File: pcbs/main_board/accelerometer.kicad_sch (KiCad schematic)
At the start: 3 parts, among them U2 ADXL345

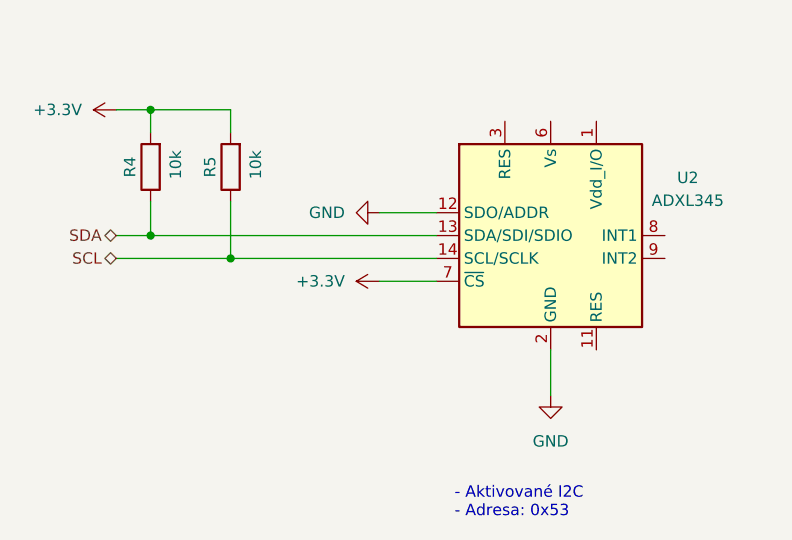
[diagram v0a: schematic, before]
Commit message: Add led strip wiring
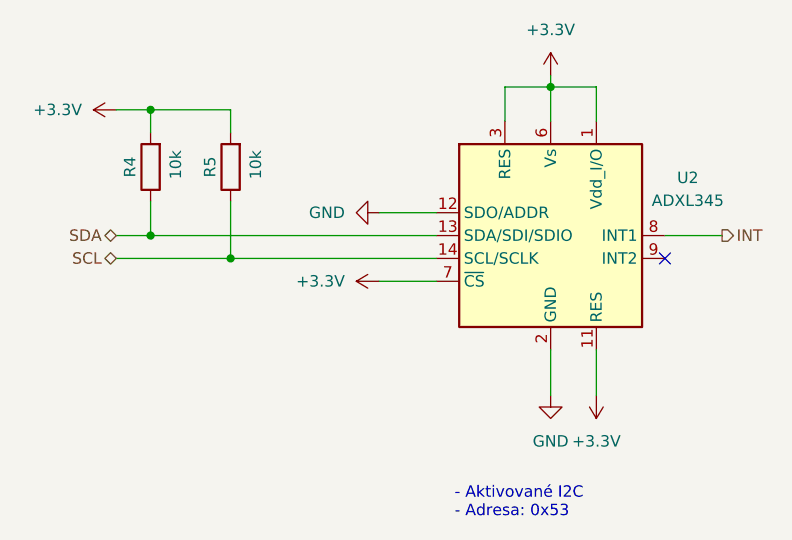
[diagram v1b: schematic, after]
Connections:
- net +3.3V: now also U2.1 (Vdd_I/O), U2.11 (RES), U2.3 (RES), U2.6 (Vs)
- net INT: now reaches U2.8 (INT1)
- no-connect marks 0 -> 1
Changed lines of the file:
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@@
+	)
+	(junction
+		(at 87.63 29.21)
+		(diameter 0)
+		(color 0 0 0 0)
 	)
 	(junction
@@
 		(color 0 0 0 0)
 	)
+	(no_connect
+		(at 100.33 48.26)
+	)
 	(wire
 		(pts
@@
 	(wire
 		(pts
+			(xy 82.55 29.21) (xy 87.63 29.21)
+		)
+		(stroke
+			(width 0)
+			(type default)
+		)
+	)
+	(wire
+		(pts
 			(xy 68.58 50.8) (xy 74.93 50.8)
 		)
@@
 	(wire
 		(pts
+			(xy 82.55 33.02) (xy 82.55 29.21)
+		)
+		(stroke
+			(width 0)
+			(type default)
+		)
+	)
+	(wire
+		(pts
 			(xy 68.58 43.18) (xy 74.93 43.18)
 		)
@@
 	(wire
 		(pts
+			(xy 92.71 58.42) (xy 92.71 63.5)
+		)
+		(stroke
+			(width 0)
+			(type default)
+		)
+	)
+	(wire
+		(pts
 			(xy 87.63 58.42) (xy 87.63 63.5)
 		)
@@
 	(wire
 		(pts
+			(xy 87.63 27.94) (xy 87.63 29.21)
+		)
+		(stroke
+			(width 0)
+			(type default)
+		)
+	)
+	(wire
+		(pts
+			(xy 92.71 33.02) (xy 92.71 29.21)
+		)
+		(stroke
+			(width 0)
+			(type default)
+		)
+	)
+	(wire
+		(pts
 			(xy 39.37 31.75) (xy 43.18 31.75)
 		)
@@
 	(wire
 		(pts
+			(xy 87.63 29.21) (xy 87.63 33.02)
+		)
+		(stroke
+			(width 0)
+			(type default)
+		)
+	)
+	(wire
+		(pts
 			(xy 43.18 41.91) (xy 43.18 45.72)
 		)
@@
 	(wire
 		(pts
+			(xy 100.33 45.72) (xy 106.68 45.72)
+		)
+		(stroke
+			(width 0)
+			(type default)
+		)
+	)
+	(wire
+		(pts
 			(xy 43.18 45.72) (xy 74.93 45.72)
+		)
+		(stroke
+			(width 0)
+			(type default)
+		)
+	)
+	(wire
+		(pts
+			(xy 92.71 29.21) (xy 87.63 29.21)
 		)
 		(stroke
@@
 			)
 			(justify right)
+		)
+	)
+	(hierarchical_label "INT"
+		(shape output)
+		(at 106.68 45.72 0)
+		(effects
+			(font
+				(size 1.27 1.27)
+			)
+			(justify left)
 		)
 	)
@@
 	(symbol
 		(lib_id "power:VCC")
+		(at 87.63 27.94 0)
+		(unit 1)
+		(exclude_from_sim no)
+		(in_bom yes)
+		(on_board yes)
+		(dnp no)
+		(fields_autoplaced yes)
+		(property "Reference" "#PWR028"
+			(at 87.63 31.75 0)
+			(effects
+				(font
+					(size 1.27 1.27)
+				)
+				(hide yes)
+			)
+		)
+		(property "Value" "+3.3V"
+			(at 87.63 22.86 0)
+			(effects
+				(font
+					(size 1.27 1.27)
+				)
+			)
+		)
+		(property "Footprint" ""
+			(at 87.63 27.94 0)
+			(effects
+				(font
+					(size 1.27 1.27)
+				)
+				(hide yes)
+			)
+		)
+		(property "Datasheet" ""
+			(at 87.63 27.94 0)
+			(effects
+				(font
+					(size 1.27 1.27)
+				)
+				(hide yes)
+			)
+		)
+		(property "Description" "Power symbol creates a global label with name \"VCC\""
+			(at 87.63 27.94 0)
+			(effects
+				(font
+					(size 1.27 1.27)
+				)
+				(hide yes)
+			)
+		)
+		(pin "1"
+		)
+		(instances
+			(project "main_board"
+				(path "/86b00c07-962a-4c6d-8d05-813891e412c9/ba209d61-c71a-44e2-be69-6b7f55e44949"
+					(reference "#PWR028")
+					(unit 1)
+				)
+			)
+		)
+	)
+	(symbol
+		(lib_id "power:VCC")
 		(at 39.37 31.75 90)
 		(unit 1)
@@
 					(unit 1)
 				)
+			)
+		)
+	)
+	(symbol
+		(lib_id "power:VCC")
+		(at 92.71 63.5 180)
+		(unit 1)
+		(exclude_from_sim no)
+		(in_bom yes)
+		(on_board yes)
+		(dnp no)
+		(fields_autoplaced yes)
+		(property "Reference" "#PWR029"
+			(at 92.71 59.69 0)
+			(effects
+				(font
+					(size 1.27 1.27)
+				)
+				(hide yes)
+			)
+		)
+		(property "Value" "+3.3V"
+			(at 92.71 68.58 0)
+			(effects
+				(font
+					(size 1.27 1.27)
+				)
+			)
+		)
+		(property "Footprint" ""
+			(at 92.71 63.5 0)
+			(effects
+				(font
+					(size 1.27 1.27)
+				)
+				(hide yes)
+			)
+		)
+		(property "Datasheet" ""
+			(at 92.71 63.5 0)
+			(effects
+				(font
+					(size 1.27 1.27)
+				)
+				(hide yes)
+			)
+		)
+		(property "Description" "Power symbol creates a global label with name \"VCC\""
+			(at 92.71 63.5 0)
+			(effects
+				(font
+					(size 1.27 1.27)
+				)
+				(hide yes)
+			)
+		)
+		(pin "1"
+		)
+		(instances
+			(project "main_board"
+				(path "/86b00c07-962a-4c6d-8d05-813891e412c9/ba209d61-c71a-44e2-be69-6b7f55e44949"
+					(reference "#PWR029")
+					(unit 1)
+				)

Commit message: Main board final update
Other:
- company: (none) -> Brno Mars Rover
- title: (none) -> Main board - MyMachine LED cap
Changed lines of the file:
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@@
 	(generator "eeschema")
 	(generator_version "9.0")
-	(paper "A5")
+	(paper "A4")
+	(title_block
+		(title "Main board - MyMachine LED cap")
+		(date "2026-01-20")
+		(company "Brno Mars Rover")
+	)
 	(text "- Aktivované I2C\n- Adresa: 0x53"
 		(exclude_from_sim no)

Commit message: Fix bom errors - main board
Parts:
- R4, R5: Manufacturer Part Number CRCW0603910KFKEAHP -> CRCW060310K0FKEI; Supplier Part Number 71-CRCW0603910KFKEAH -> 71-CRCW060310K0FKEI
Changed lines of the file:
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@@
 			)
 		)
-		(property "Manufacturer Part Number" "CRCW0603910KFKEAHP"
+		(property "Manufacturer Part Number" "CRCW060310K0FKEI"
 			(at 43.18 38.1 90)
 			(effects
@@
 			)
 		)
-		(property "Supplier Part Number" "71-CRCW0603910KFKEAH"
+		(property "Supplier Part Number" "71-CRCW060310K0FKEI"
 			(at 43.18 38.1 90)
 			(effects
@@
 			)
 		)
-		(property "Manufacturer Part Number" "CRCW0603910KFKEAHP"
+		(property "Manufacturer Part Number" "CRCW060310K0FKEI"
 			(at 52.07 38.1 90)
 			(effects
@@
 			)
 		)
-		(property "Supplier Part Number" "71-CRCW0603910KFKEAH"
+		(property "Supplier Part Number" "71-CRCW060310K0FKEI"
 			(at 52.07 38.1 90)
 			(effects
